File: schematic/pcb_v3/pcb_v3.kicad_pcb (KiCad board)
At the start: 4 copper layers, 56 x 56 mm, 54 parts, among them IC1 FT232RNQ-TRAY, J1 5V, J2 SERVO, J3 MAVLINK, J4 DISPLAY, J5 SER. SERVO, J6 MAG., J7 U.FL-R, J9 Conn_01x05_Pin, P1 USB_C_Plug_USB2.0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

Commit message: status screen
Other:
- board text added: "GPS BACKUP"

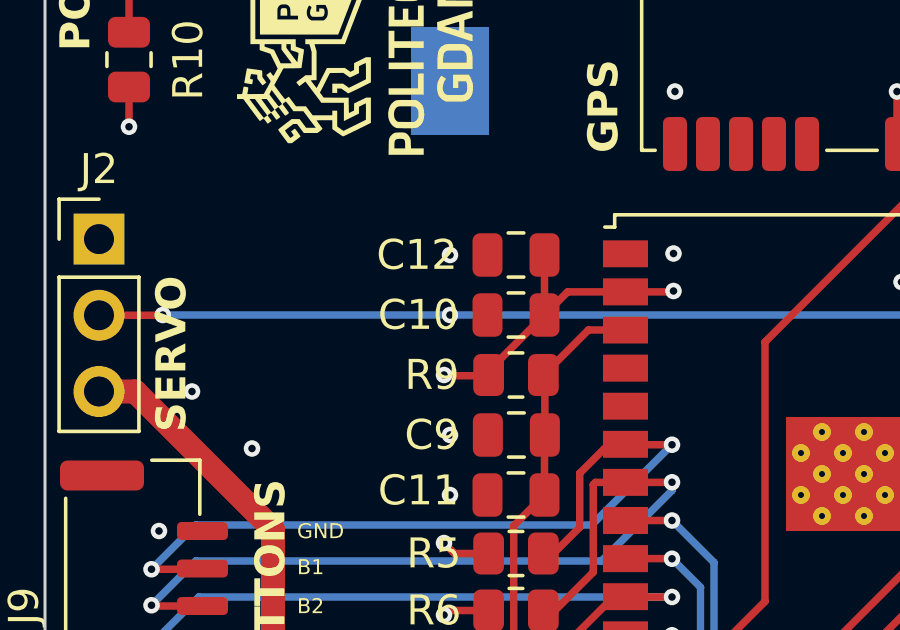
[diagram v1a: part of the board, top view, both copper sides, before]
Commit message: pcb bad via, tests
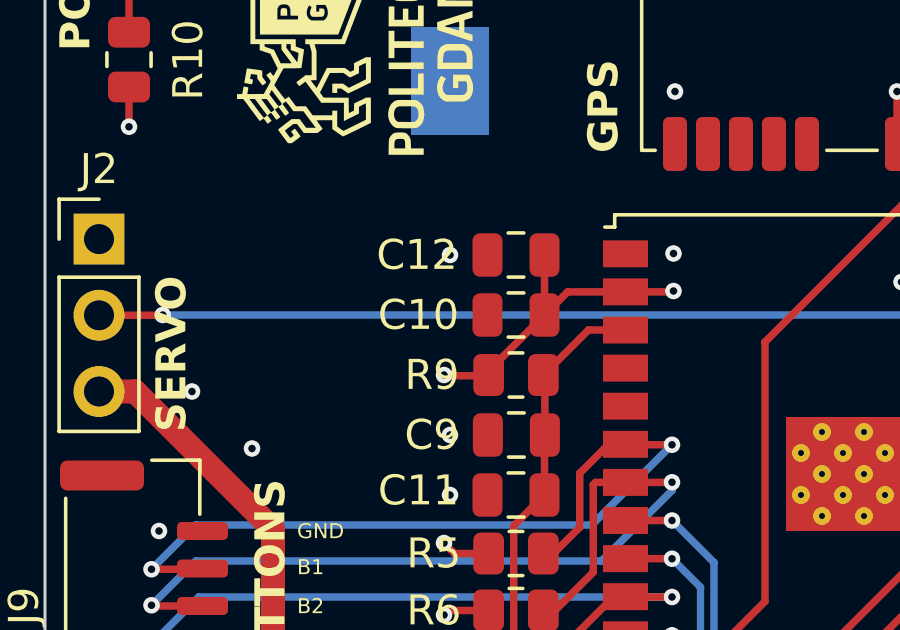
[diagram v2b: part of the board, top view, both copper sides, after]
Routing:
- net GND: vias 60 -> 59
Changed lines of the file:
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@@
   (via (at 217.74941 93.24941) (size 0.55) (drill 0.25) (layers "F.Cu" "B.Cu") (free) (net 2))
   (via (at 206.2 53.3) (size 0.55) (drill 0.25) (layers "F.Cu" "B.Cu") (free) (net 2))
-  (via (at 200.5 67.3) (size 0.55) (drill 0.25) (layers "F.Cu" "B.Cu") (free) (net 2))
   (via (at 214.9 90.45) (size 0.55) (drill 0.25) (layers "F.Cu" "B.Cu") (free) (net 2))
   (via (at 225.25 65.25) (size 0.55) (drill 0.25) (layers "F.Cu" "B.Cu") (free) (net 2))

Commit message: pcb update
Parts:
- added J8: Conn_01x05_Pin, Connector_PinHeader_1.27mm:PinHeader_1x05_P1.27mm_Vertical_SMD_Pin1Left, F.Cu at (13.6, 3.73)
- added SW2: SW_Push, Button_Switch_SMD:SW_SPST_B3SL-1002P, F.Cu at (4.53, 3.67)
- added SW3: SW_Push, Button_Switch_SMD:SW_SPST_B3SL-1002P, F.Cu at (4.53, 12.0)
- added SW4: SW_Push, Button_Switch_SMD:SW_SPST_B3SL-1002P, F.Cu at (4.53, 20.4)
- added SW5: SW_Push, Button_Switch_SMD:SW_SPST_B3SL-1002P, F.Cu at (4.53, 28.7)
- added U3: FM24C64B, Package_DFN_QFN:DFN-8_2x2mm_P0.5mm, F.Cu at (227.6, 69.8)
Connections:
- net MAG_SCK renamed SCK
- net MAG_SDI renamed SDI
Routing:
- net SCK: track 22.3 -> 30.5 mm
- net SDI: track 27.9 -> 34.7 mm
- net SCREEN_CS: track 21.0 -> 16.9 mm
- net SCREEN_SCK: track 20.2 -> 16.9 mm
- net GND: track 35.5 -> 38.1 mm, vias 59 -> 61
- net +3V3: track 39.2 -> 40.1 mm, vias 14 -> 15

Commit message: fram, gps uart
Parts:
- removed G***: LOGO, LOGO
- added J10: UART/SPI, Connector_PinHeader_2.54mm:PinHeader_1x02_P2.54mm_Vertical, F.Cu at (231.8, 48.8)
- added J11: Conn_01x03_Pin, Connector_PinHeader_2.54mm:PinHeader_1x03_P2.54mm_Vertical, F.Cu at (196.9, 55.5)
- added R12: 2.2K, Resistor_SMD:R_0805_2012Metric, F.Cu at (230.7, 55.0)
- added R13: 2.2K, Resistor_SMD:R_0805_2012Metric, F.Cu at (230.7, 56.9)
- moved U3 1.00 mm to (227.8, 70.7)
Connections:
- net GPS_MISO renamed GPS_MISO/TX
- net GPS_MOSI renamed GPS_MOSI/RX
- J2 pad 2: SERVO -> +5V
- J2 pad 3: +5V -> SERVO
- U1 pad 2: GND -> Net-(J10-Pin_1)
- U3 pad 1: unconnected-(U3-A0-Pad1) -> GND
- U3 pad 2: unconnected-(U3-A1-Pad2) -> GND
- U3 pad 3: unconnected-(U3-A2-Pad3) -> GND
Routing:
- net GPS_MOSI/RX: track 24.8 -> 48.4 mm
- net GPS_MISO/TX: track 26.8 -> 49.3 mm
- net Net-(J10-Pin_1): track 0.00 -> 16.4 mm
- net SCK: track 30.5 -> 41.6 mm
- net +3V3: track 40.1 -> 48.0 mm
- net SDI: track 34.7 -> 39.5 mm
- net +5V: track 134.9 -> 137.4 mm
- net SERVO: track 48.6 -> 49.7 mm
- net Net-(U1-TIMEPULSE): track 6.43 -> 7.05 mm
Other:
- board text added: "FRAM"
- board text added: "GPS UART"
- board text added: "TRACKER PCB v. beta v4 10/2024"
- board text added: "UART/SPI"
- board text removed: "TRACKER PCB v. beta v3 6/2024"

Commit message: pcb cleanup
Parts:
- removed J8: Conn_01x05_Pin, Connector_PinHeader_1.27mm:PinHeader_1x05_P1.27mm_Vertical_SMD_Pin1Left
- removed SW2, SW3, SW4, SW5: SW_Push, Button_Switch_SMD:SW_SPST_B3SL-1002P
- moved U3 2.06 mm to (229.8, 70.8)
- moved R13 1.08 mm to (229.6, 57.0)
- moved R12 1.08 mm to (229.6, 55.0)
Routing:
- net SCK: track 41.6 -> 45.5 mm
- net SDI: track 39.5 -> 42.6 mm
- net GPS_MISO/TX: track 49.3 -> 51.9 mm
- net GPS_MOSI/RX: track 48.4 -> 50.4 mm
- net +3V3: track 48.0 -> 46.9 mm
- net SCREEN_CS: track 16.9 -> 17.8 mm
- net SCREEN_SCK: track 16.9 -> 17.5 mm
- net GND: vias 61 -> 62
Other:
- board text added: "R"
- board text added: "T"

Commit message: final pcb please
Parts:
- added TP1: TestPoint, TestPoint:TestPoint_Pad_D1.5mm, F.Cu at (226.8, 69.7)
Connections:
- REF** pad 1: (no net) -> GND (x4)
- U3 pad 1: GND -> Net-(U3-A0)
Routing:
- net GND: track 38.1 -> 24.6 mm, vias 62 -> 28
- net +3V3: track 46.9 -> 55.1 mm, vias 15 -> 9
- net +5V: track 137.4 -> 132.1 mm, vias 0 -> 2
- net SERVO: track 49.7 -> 53.1 mm
- net IO0: track 41.1 -> 43.5 mm
- net Net-(U3-A0): track 0.00 -> 2.19 mm
- net Net-(J10-Pin_1): track 16.4 -> 15.9 mm
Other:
- board text added: "3V3"
- board text added: "3V3 LDO"
- board text added: "GPS BACKUP CR2032"
- board text added: "USB-UART"
- board text removed: "3V"
- board text removed: "GPS BACKUP"

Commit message: magnetometer interface, cleanup
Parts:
- removed TP1: TestPoint, TestPoint:TestPoint_Pad_D1.5mm
- added J8: Conn_01x05_Pin, Connector_PinHeader_1.27mm:PinHeader_1x05_P1.27mm_Vertical_SMD_Pin1Left, F.Cu at (13.6, 3.73)
- added SW2: SW_Push, Button_Switch_SMD:SW_SPST_B3SL-1002P, F.Cu at (4.53, 3.67)
- added SW3: SW_Push, Button_Switch_SMD:SW_SPST_B3SL-1002P, F.Cu at (4.53, 12.0)
- added SW4: SW_Push, Button_Switch_SMD:SW_SPST_B3SL-1002P, F.Cu at (4.53, 20.4)
- added SW5: SW_Push, Button_Switch_SMD:SW_SPST_B3SL-1002P, F.Cu at (4.53, 28.7)
- U3: footprint Package_DFN_QFN:DFN-8_2x2mm_P0.5mm -> Package_SON:SON95P400X450X80-9N
- moved U3 1.47 mm to (228.5, 71.4)
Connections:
- U3 pad 1: Net-(U3-A0) -> unconnected-(U3-A0-Pad1)
- U3 pad 2: GND -> unconnected-(U3-A1-Pad2)
- U3 pad 3: GND -> unconnected-(U3-A2-Pad3)
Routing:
- net GND: track 24.6 -> 20.8 mm, vias 28 -> 29
- net SDI: track 42.6 -> 45.2 mm
- net Net-(U3-A0): track 2.19 -> 0.00 mm
- net SCK: track 45.5 -> 46.5 mm
- net +3V3: track 55.1 -> 55.9 mm

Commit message: tests
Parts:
- added C16: 100nF, Capacitor_SMD:C_0805_2012Metric, F.Cu at (202.4, 55.1)
- added L1: 27nH, Inductor_SMD:L_0805_2012Metric, F.Cu at (203.3, 52.3)
- added R14: 20, Resistor_SMD:R_0805_2012Metric, F.Cu at (205.2, 54.3)
- moved J7 3.28 mm to (203.3, 48.8), turned to 0 degrees
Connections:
- U1 pad 9: unconnected-(U1-VCC_RF-Pad9) -> Net-(U1-VCC_RF)
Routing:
- net Net-(U1-VCC_RF): track 0.00 -> 9.13 mm
- net Net-(C16-Pad2): track 0.00 -> 3.69 mm
- net Net-(U1-RF_IN): track 4.88 -> 7.02 mm
- net GND: vias 29 -> 41
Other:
- board text added: "TRACKER PCB v. beta v5 11/2024"
- board text removed: "TRACKER PCB v. beta v4 10/2024"
